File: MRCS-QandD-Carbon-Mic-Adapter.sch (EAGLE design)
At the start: 9 parts, among them CON1 DC PWR, CON2 Output

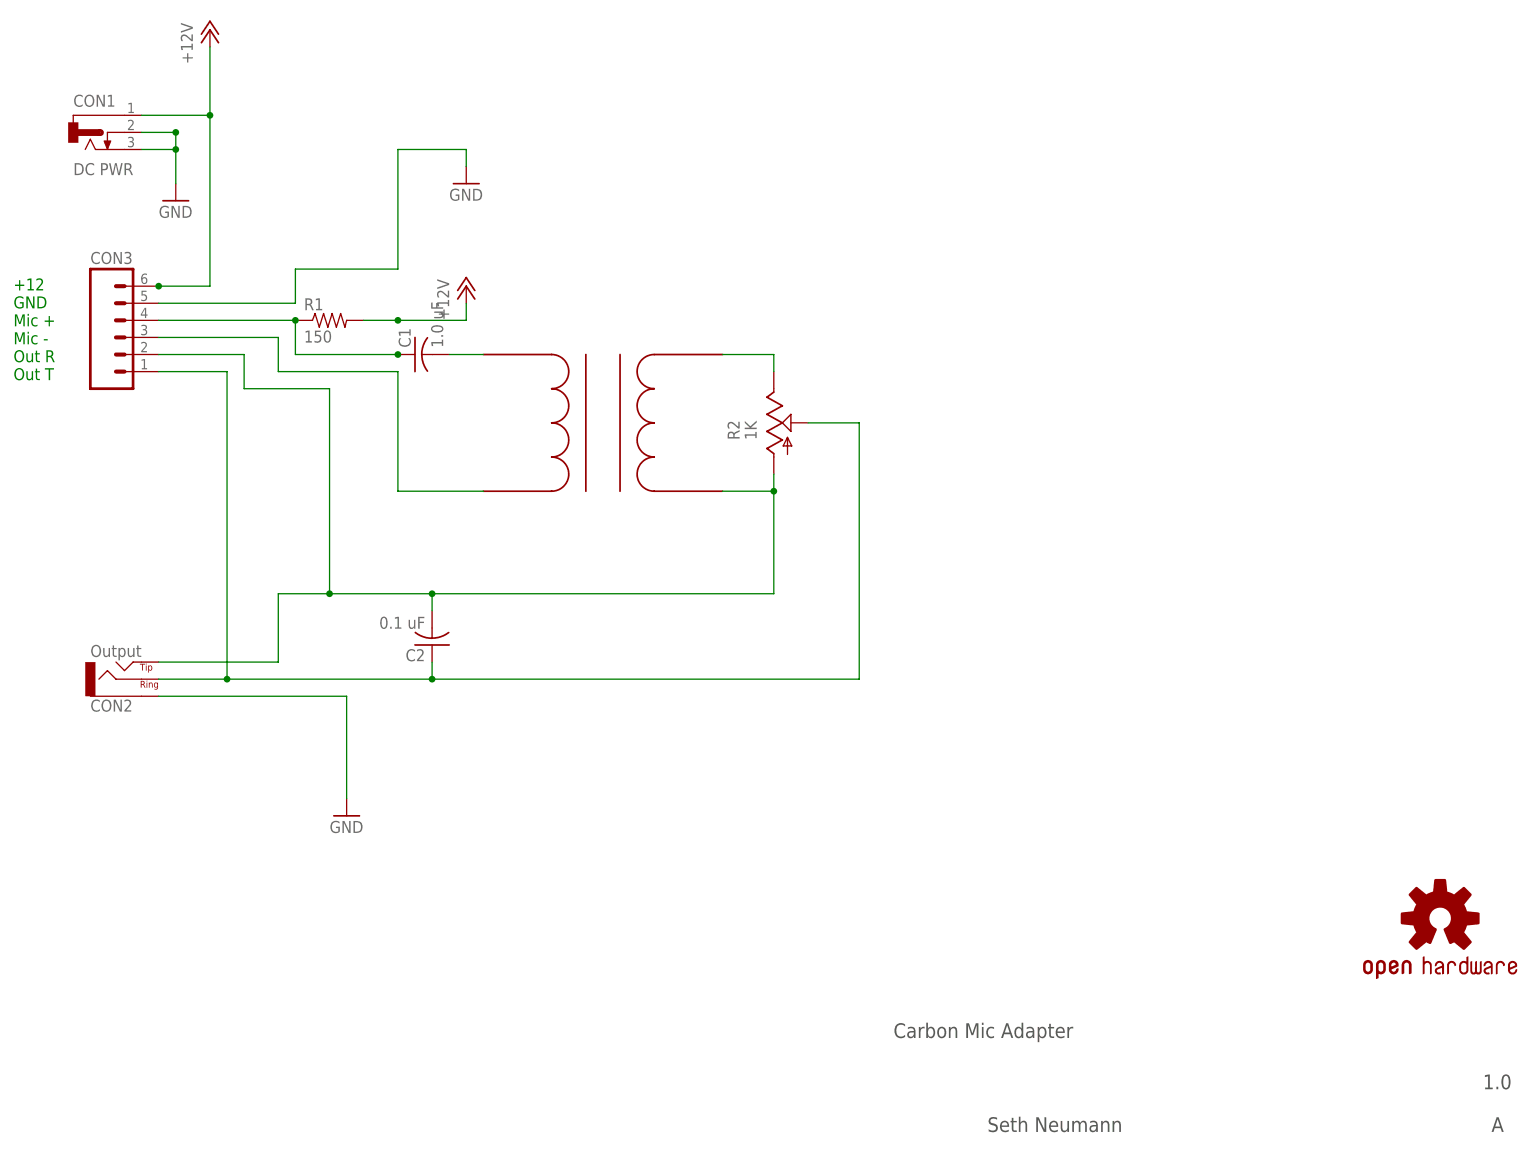
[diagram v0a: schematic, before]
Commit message: Version 1.1 fixed input ground, general cleanup
Version 1.1 fixed input ground, general cleanup
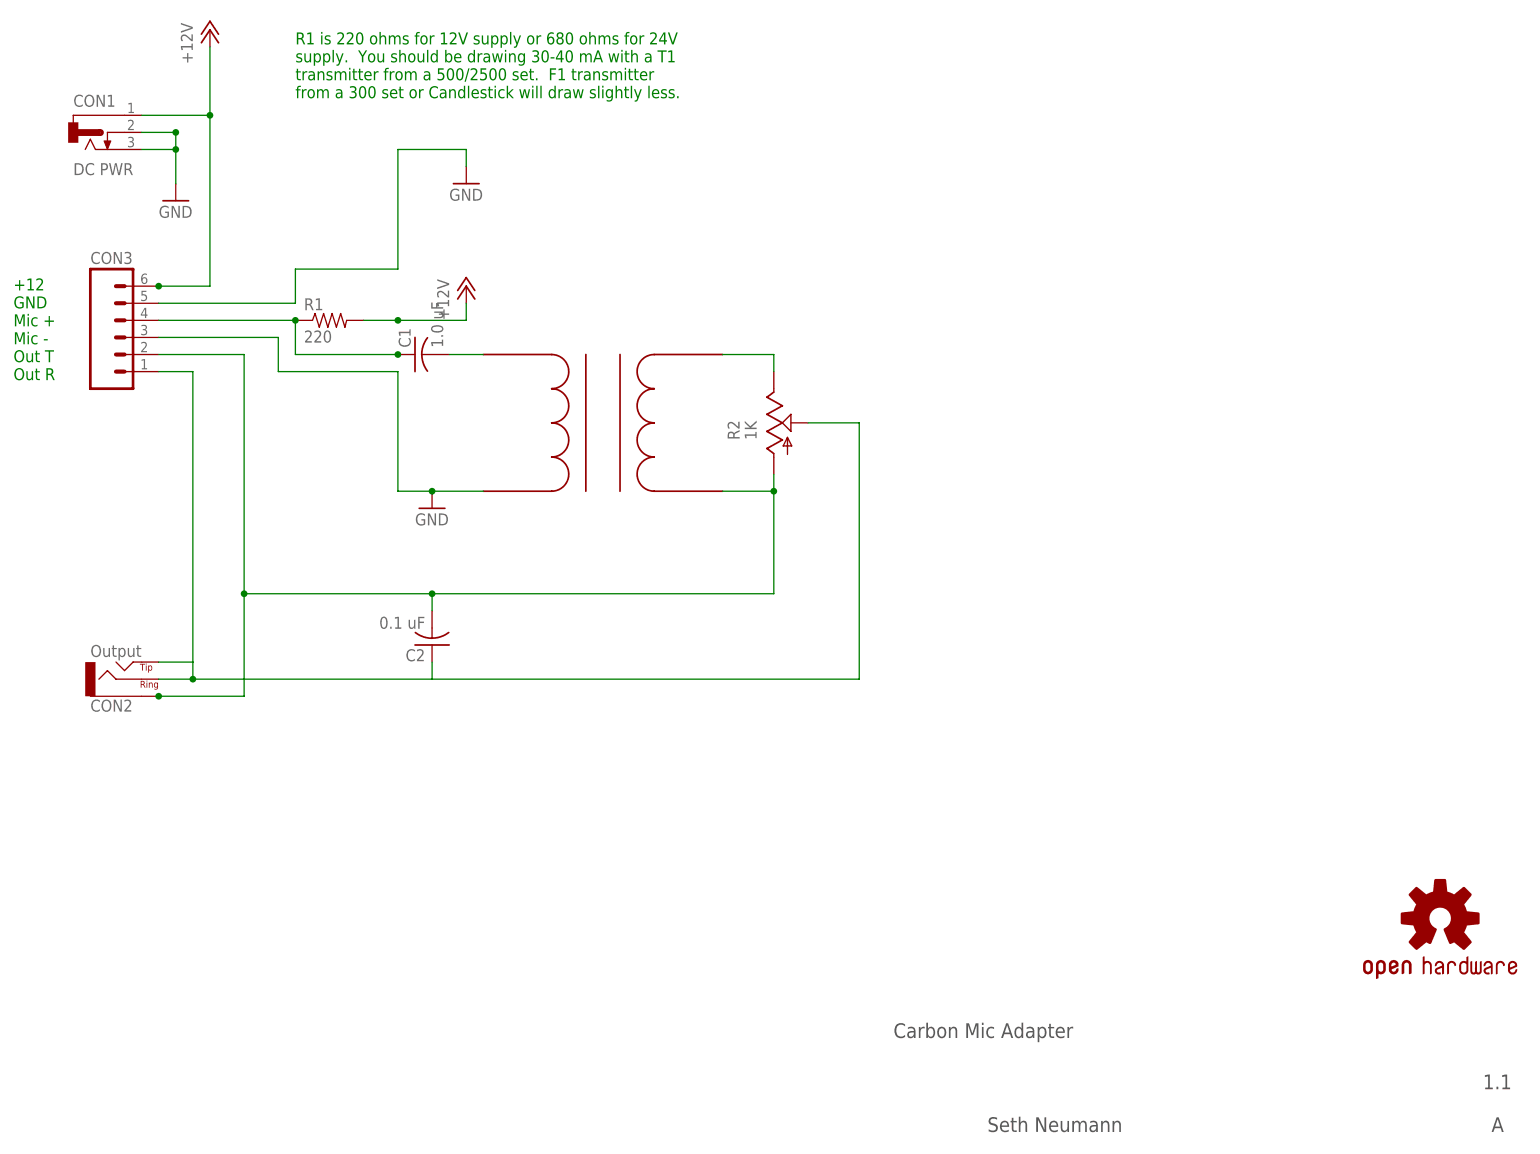
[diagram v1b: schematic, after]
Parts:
- R1: value 150 -> 220
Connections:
- removed net OUTR: CON3.3, U$1.PBOTTOM
- net GND: now also CON3.3, U$1.PBOTTOM; no longer CON2.SLEEVE
- net N$7: now also CON2.TIP
- net OUTT: now also CON2.SLEEVE; no longer CON2.TIP
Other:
- note added: "+12 GND Mic + Mic - Out T Out R"
- note added: "1.1"
- note added: "R1 is 220 ohms for 12V supply or 680 ohms for 24V supply. You should be drawing 30-40 mA with a T1 transmitter from a 500/2500 set. F1 transmitter from a 300 set or Candlestick will draw slightly less."
- note removed: "+12 GND Mic + Mic - Out R Out T"
- note removed: "1.0"
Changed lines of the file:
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@@
 <part name="C1" library="SPCoast" deviceset="CAP*" device="PTH2" value="1.0 uF"/>
 <part name="GND1" library="SPCoast" deviceset="GND" device=""/>
-<part name="R1" library="SPCoast" deviceset="R*" device="PTH04" value="150"/>
+<part name="R1" library="SPCoast" deviceset="R*" device="PTH04" value="220"/>
 <part name="CON2" library="SPCoast" deviceset="CONNECTOR-AUDIO" device="3.5MM-ADAMTECH" value="Output"/>
 <part name="U$1" library="MRCS" deviceset="EI14_600-600" device=""/>
@@
 <part name="CON1" library="SPCoast" deviceset="CONNECTOR-DC-POWER" device="-RA" value="DC PWR"/>
 <part name="GND2" library="SPCoast" deviceset="GND" device=""/>
-<part name="GND3" library="SPCoast" deviceset="GND" device=""/>
 <part name="P+2" library="SPCoast" deviceset="+12V" device=""/>
 <part name="R2" library="pot" deviceset="TRIM_US-" device="RS3" value="1K"/>
 <part name="C2" library="SPCoast" deviceset="CAP*" device="PTH2" value="0.1 uF"/>
+<part name="GND4" library="SPCoast" deviceset="GND" device=""/>
 </parts>
 <sheets>
@@
 <plain>
 <text x="152.4" y="20.32" size="2.1844" layer="97">Carbon Mic Adapter</text>
-<text x="240.03" y="12.7" size="2.1844" layer="97">1.0</text>
+<text x="240.03" y="12.7" size="2.1844" layer="97">1.1</text>
 <text x="241.3" y="6.35" size="2.1844" layer="97">A</text>
 <text x="166.37" y="6.35" size="2.1844" layer="97">Seth Neumann</text>
@@
 Mic +
 Mic -
-Out R
-Out T</text>
+Out T
+Out R</text>
+<text x="63.5" y="160.02" size="1.778" layer="91">R1 is 220 ohms for 12V supply or 680 ohms for 24V
+supply.  You should be drawing 30-40 mA with a T1
+transmitter from a 500/2500 set.  F1 transmitter
+from a 300 set or Candlestick will draw slightly less.</text>
 </plain>
 <instances>
@@
 <instance part="CON1" gate="J" x="33.02" y="154.94"/>
 <instance part="GND2" gate="1" x="45.72" y="144.78"/>
-<instance part="GND3" gate="1" x="71.12" y="53.34"/>
 <instance part="P+2" gate="1" x="88.9" y="132.08"/>
 <instance part="R2" gate="G$1" x="134.62" y="111.76"/>
 <instance part="C2" gate="C1" x="83.82" y="78.74" rot="R180"/>
+<instance part="GND4" gate="1" x="83.82" y="99.06"/>
 </instances>
 <busses>
@@
 </segment>
 <segment>
-<wire x1="43.18" y1="71.12" x2="71.12" y2="71.12" width="0.6096" layer="91"/>
-<pinref part="CON2" gate="J" pin="SLEEVE"/>
-<pinref part="GND3" gate="1" pin="GND"/>
-<wire x1="71.12" y1="71.12" x2="71.12" y2="55.88" width="0.6096" layer="91"/>
-</segment>
-<segment>
 <wire x1="78.74" y1="134.62" x2="78.74" y2="152.4" width="0.6096" layer="91"/>
 <wire x1="78.74" y1="152.4" x2="88.9" y2="152.4" width="0.6096" layer="91"/>
@@
 <wire x1="63.5" y1="129.54" x2="63.5" y2="134.62" width="0.6096" layer="91"/>
 <wire x1="63.5" y1="134.62" x2="78.74" y2="134.62" width="0.6096" layer="91"/>
+</segment>
+<segment>
+<pinref part="CON3" gate="J" pin="3"/>
+<wire x1="43.18" y1="124.46" x2="60.96" y2="124.46" width="0.6096" layer="91"/>
+<wire x1="60.96" y1="124.46" x2="60.96" y2="119.38" width="0.6096" layer="91"/>
+<wire x1="60.96" y1="119.38" x2="78.74" y2="119.38" width="0.6096" layer="91"/>
+<wire x1="78.74" y1="119.38" x2="78.74" y2="101.6" width="0.6096" layer="91"/>
+<pinref part="U$1" gate="G$1" pin="PBOTTOM"/>
+<wire x1="78.74" y1="101.6" x2="83.82" y2="101.6" width="0.6096" layer="91"/>
+<pinref part="GND4" gate="1" pin="GND"/>
+<wire x1="83.82" y1="101.6" x2="91.44" y2="101.6" width="0.6096" layer="91"/>
+<junction x="83.82" y="101.6"/>
 </segment>
 </net>
@@
 </segment>
 </net>
-<net name="OUTR" class="0">
-<segment>
-<pinref part="CON3" gate="J" pin="3"/>
-<wire x1="43.18" y1="124.46" x2="60.96" y2="124.46" width="0.6096" layer="91"/>
-<wire x1="60.96" y1="124.46" x2="60.96" y2="119.38" width="0.6096" layer="91"/>
-<wire x1="60.96" y1="119.38" x2="78.74" y2="119.38" width="0.6096" layer="91"/>
-<wire x1="78.74" y1="119.38" x2="78.74" y2="101.6" width="0.6096" layer="91"/>
-<pinref part="U$1" gate="G$1" pin="PBOTTOM"/>
-<wire x1="78.74" y1="101.6" x2="91.44" y2="101.6" width="0.6096" layer="91"/>
-</segment>
-</net>
 <net name="N$1" class="0">
 <segment>
@@
 <wire x1="127" y1="101.6" x2="134.62" y2="101.6" width="0.4064" layer="91"/>
 <wire x1="134.62" y1="101.6" x2="134.62" y2="104.14" width="0.4064" layer="91"/>
-<pinref part="CON2" gate="J" pin="TIP"/>
-<wire x1="43.18" y1="76.2" x2="60.96" y2="76.2" width="0.4064" layer="91"/>
-<wire x1="60.96" y1="76.2" x2="60.96" y2="86.36" width="0.4064" layer="91"/>
-<wire x1="60.96" y1="86.36" x2="68.58" y2="86.36" width="0.4064" layer="91"/>
-<wire x1="68.58" y1="86.36" x2="83.82" y2="86.36" width="0.4064" layer="91"/>
+<wire x1="55.88" y1="86.36" x2="83.82" y2="86.36" width="0.4064" layer="91"/>
 <wire x1="83.82" y1="86.36" x2="134.62" y2="86.36" width="0.4064" layer="91"/>
 <wire x1="134.62" y1="86.36" x2="134.62" y2="101.6" width="0.4064" layer="91"/>
 <pinref part="CON3" gate="J" pin="2"/>
 <wire x1="43.18" y1="121.92" x2="55.88" y2="121.92" width="0.4064" layer="91"/>
-<wire x1="55.88" y1="121.92" x2="55.88" y2="116.84" width="0.4064" layer="91"/>
-<wire x1="55.88" y1="116.84" x2="68.58" y2="116.84" width="0.4064" layer="91"/>
-<wire x1="68.58" y1="116.84" x2="68.58" y2="86.36" width="0.4064" layer="91"/>
-<junction x="68.58" y="86.36"/>
+<wire x1="55.88" y1="121.92" x2="55.88" y2="86.36" width="0.4064" layer="91"/>
+<junction x="55.88" y="86.36"/>
 <junction x="134.62" y="101.6"/>
 <pinref part="C2" gate="C1" pin="2"/>
 <wire x1="83.82" y1="83.82" x2="83.82" y2="86.36" width="0.4064" layer="91"/>
 <junction x="83.82" y="86.36"/>
+<pinref part="CON2" gate="J" pin="SLEEVE"/>
+<junction x="43.18" y="71.12"/>
+<wire x1="43.18" y1="71.12" x2="55.88" y2="71.12" width="0.4064" layer="91"/>
+<wire x1="55.88" y1="71.12" x2="55.88" y2="86.36" width="0.4064" layer="91"/>
 </segment>
 </net>
 <net name="N$7" class="0">
 <segment>
-<pinref part="CON2" gate="J" pin="RING"/>
-<wire x1="43.18" y1="73.66" x2="53.34" y2="73.66" width="0.4064" layer="91"/>
-<wire x1="53.34" y1="73.66" x2="83.82" y2="73.66" width="0.4064" layer="91"/>
 <wire x1="83.82" y1="73.66" x2="147.32" y2="73.66" width="0.4064" layer="91"/>
 <wire x1="147.32" y1="73.66" x2="147.32" y2="111.76" width="0.4064" layer="91"/>
 <pinref part="R2" gate="G$1" pin="S"/>
 <wire x1="147.32" y1="111.76" x2="139.7" y2="111.76" width="0.4064" layer="91"/>
-<pinref part="CON3" gate="J" pin="1"/>
-<wire x1="43.18" y1="119.38" x2="53.34" y2="119.38" width="0.4064" layer="91"/>
-<wire x1="53.34" y1="119.38" x2="53.34" y2="73.66" width="0.4064" layer="91"/>
-<junction x="53.34" y="73.66"/>
 <pinref part="C2" gate="C1" pin="1"/>
 <wire x1="83.82" y1="76.2" x2="83.82" y2="73.66" width="0.4064" layer="91"/>
-<junction x="83.82" y="73.66"/>
+<pinref part="CON2" gate="J" pin="TIP"/>
+<wire x1="43.18" y1="76.2" x2="48.26" y2="76.2" width="0.4064" layer="91"/>
+<wire x1="48.26" y1="73.66" x2="48.26" y2="76.2" width="0.4064" layer="91"/>
+<pinref part="CON2" gate="J" pin="RING"/>
+<wire x1="43.18" y1="73.66" x2="48.26" y2="73.66" width="0.4064" layer="91"/>
+<wire x1="83.82" y1="73.66" x2="48.26" y2="73.66" width="0.4064" layer="91"/>
+<junction x="48.26" y="73.66"/>
+<pinref part="CON3" gate="J" pin="1"/>
+<wire x1="43.18" y1="119.38" x2="48.26" y2="119.38" width="0.4064" layer="91"/>
+<wire x1="48.26" y1="76.2" x2="48.26" y2="119.38" width="0.4064" layer="91"/>
 </segment>
 </net>
